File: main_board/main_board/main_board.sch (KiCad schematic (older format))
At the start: 9 parts, among them J1 jstsh4x1, J2 3.3v bus, J3 GND_bus, U1 Teensy3.5_All_Pins

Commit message: updated daughter board holes, should be good to fab
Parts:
- H1, H2, H3, H4: footprint exocam_charge_amp:mount_hole_2.5mm -> exocam_charge_amp:mount_hole_3mm
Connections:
- wire segments 31 -> 30
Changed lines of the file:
@@
 	1    0    0    -1
 $EndComp
-Wire Wire Line
-	3750 5300 3950 5300
 $Comp
 L power:GND #PWR0114
@@
 F 0 "H1" H 6900 2646 50  0000 L CNN
 F 1 "MountingHole-Mechanical" H 6900 2555 50  0000 L CNN
-F 2 "exocam_charge_amp:mount_hole_2.5mm" H 6800 2600 50  0001 C CNN
+F 2 "exocam_charge_amp:mount_hole_3mm" H 6800 2600 50  0001 C CNN
 F 3 "" H 6800 2600 50  0001 C CNN
 	1    6800 2600
@@
 F 0 "H2" H 6900 2896 50  0000 L CNN
 F 1 "MountingHole-Mechanical" H 6900 2805 50  0000 L CNN
-F 2 "exocam_charge_amp:mount_hole_2.5mm" H 6800 2850 50  0001 C CNN
+F 2 "exocam_charge_amp:mount_hole_3mm" H 6800 2850 50  0001 C CNN
 F 3 "" H 6800 2850 50  0001 C CNN
 	1    6800 2850
@@
 F 0 "H3" H 6900 3146 50  0000 L CNN
 F 1 "MountingHole-Mechanical" H 6900 3055 50  0000 L CNN
-F 2 "exocam_charge_amp:mount_hole_2.5mm" H 6800 3100 50  0001 C CNN
+F 2 "exocam_charge_amp:mount_hole_3mm" H 6800 3100 50  0001 C CNN
 F 3 "" H 6800 3100 50  0001 C CNN
 	1    6800 3100
@@
 F 0 "H4" H 6900 3396 50  0000 L CNN
 F 1 "MountingHole-Mechanical" H 6900 3305 50  0000 L CNN
-F 2 "exocam_charge_amp:mount_hole_2.5mm" H 6800 3350 50  0001 C CNN
+F 2 "exocam_charge_amp:mount_hole_3mm" H 6800 3350 50  0001 C CNN
 F 3 "" H 6800 3350 50  0001 C CNN
 	1    6800 3350
@@
 $EndComp
 Wire Wire Line
-	3950 5300 4500 5300
-Wire Wire Line
 	4750 5300 4750 5250
-Connection ~ 3950 5300
 $Comp
 L main_board-rescue:power_bus-exocam_charge_amp J3
@@
 Wire Wire Line
 	4500 5300 4750 5300
+Wire Wire Line
+	3750 5300 4500 5300
 $EndSCHEMATC

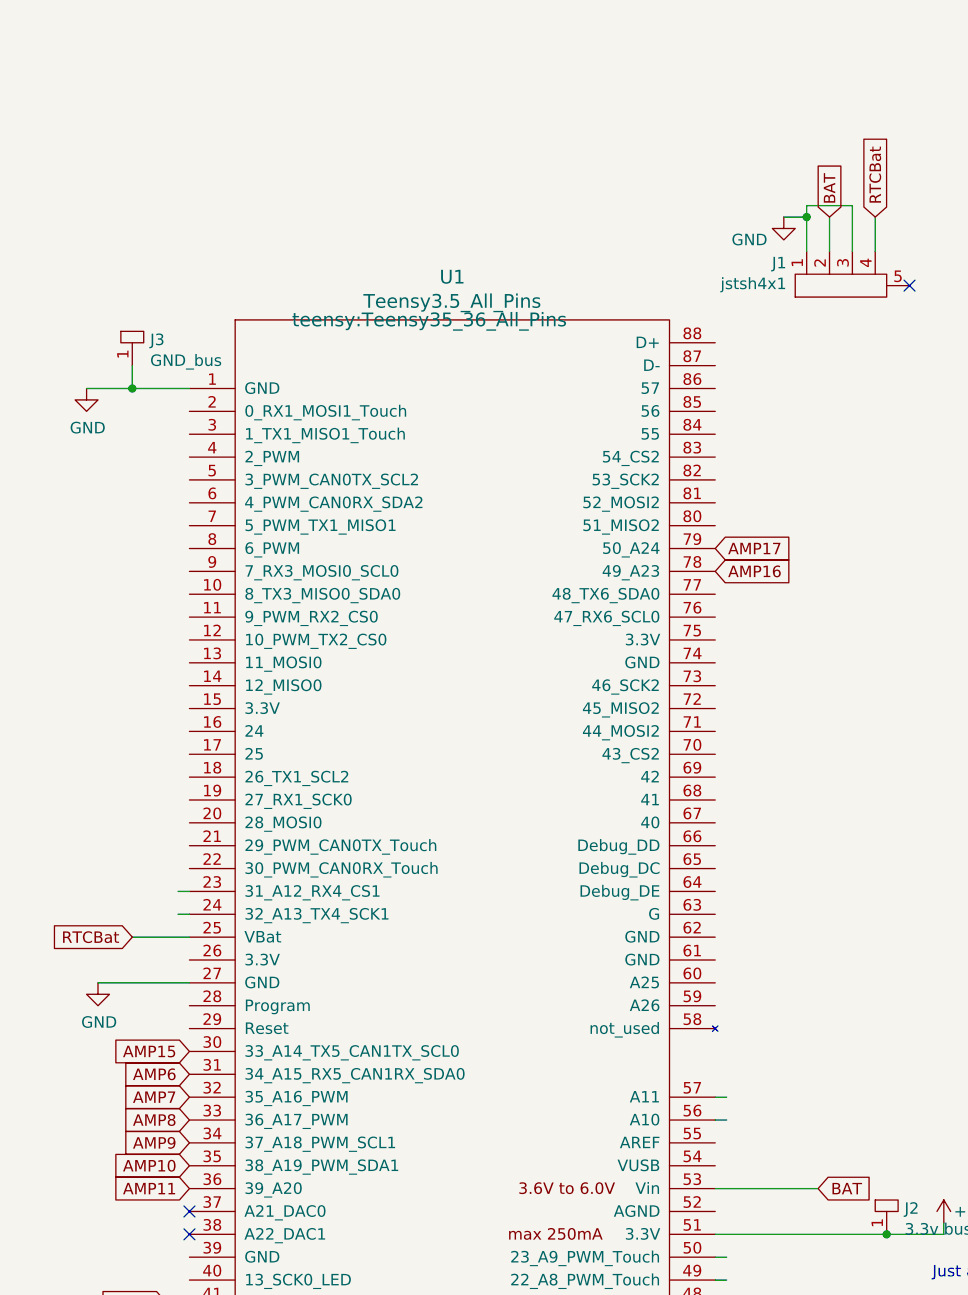
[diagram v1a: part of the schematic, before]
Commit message: edited daughter board schematic slightly to include the latest push button addition
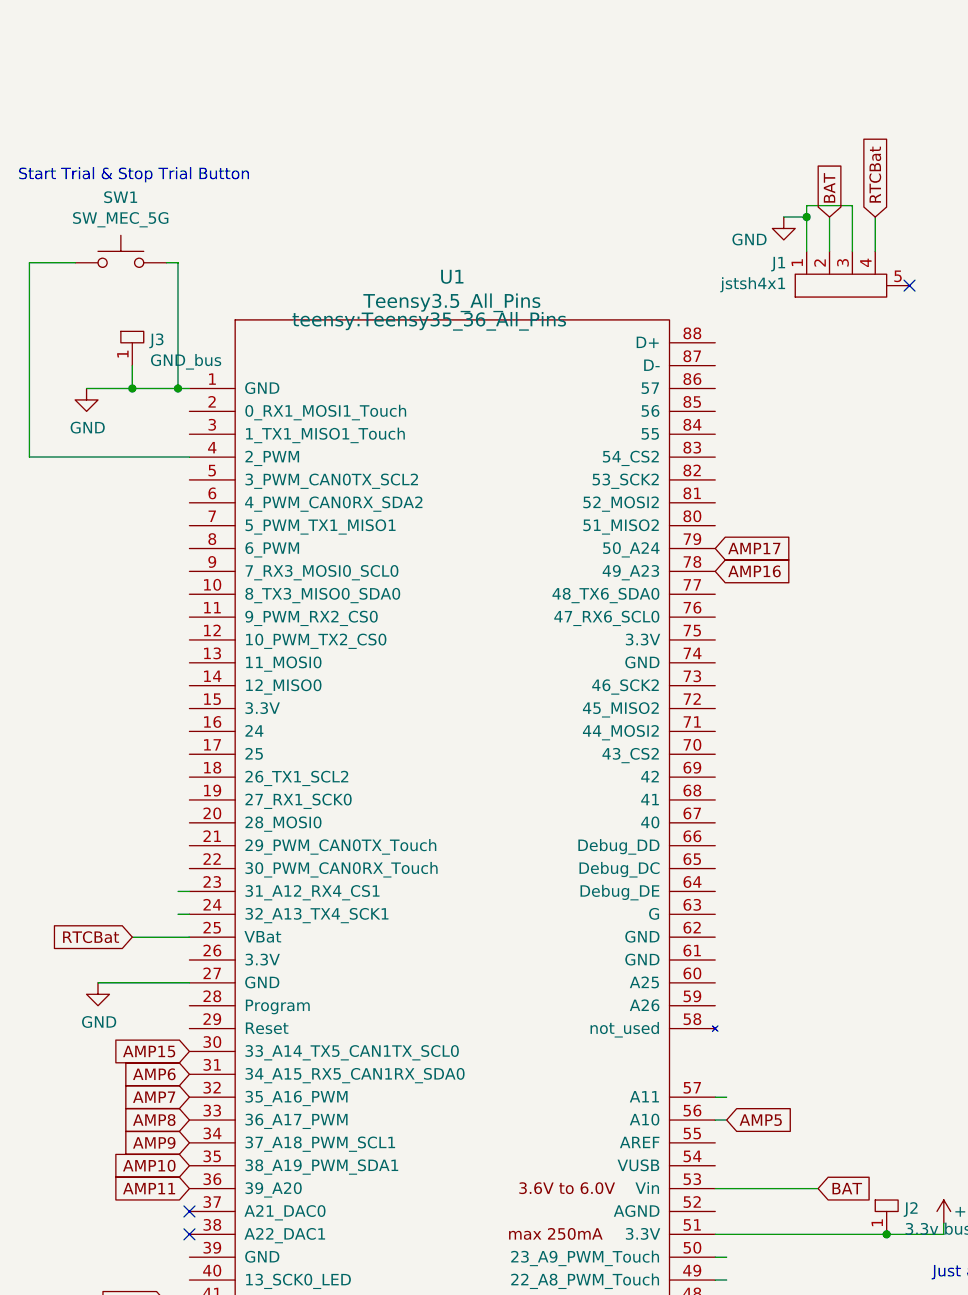
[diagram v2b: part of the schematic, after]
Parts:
- added SW1: SW_MEC_5G, symbol Switch:SW_MEC_5G
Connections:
- net labels added: AMP5
- wire segments 30 -> 36
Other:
- note added: "Start Trial & Stop Trial Button"
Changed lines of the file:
@@
 Connection ~ 1200 1600
 Wire Wire Line
-	1200 1600 1450 1600
+	1200 1600 1400 1600
 Text Notes 4700 5500 0    50   ~ 0
 Just a large ish pad that can be used for soldering a large number of wires.
@@
 Wire Wire Line
 	3750 5300 4500 5300
+Text GLabel 3800 4800 2    50   Input ~ 0
+AMP5
+$Comp
+L Switch:SW_MEC_5G SW1
+U 1 1 61235458
+P 1150 1050
+F 0 "SW1" H 1150 1335 50  0000 C CNN
+F 1 "SW_MEC_5G" H 1150 1244 50  0000 C CNN
+F 2 "" H 1150 1250 50  0001 C CNN
+F 3 "http://www.apem.com/int/index.php?controller=attachment&id_attachment=488" H 1150 1250 50  0001 C CNN
+	1    1150 1050
+	1    0    0    -1
+$EndComp
+Wire Wire Line
+	1400 1600 1400 1050
+Wire Wire Line
+	1400 1050 1350 1050
+Connection ~ 1400 1600
+Wire Wire Line
+	1400 1600 1450 1600
+Wire Wire Line
+	950  1050 750  1050
+Wire Wire Line
+	750  1050 750  1900
+Wire Wire Line
+	750  1900 1450 1900
+Text Notes 700  700  0    50   ~ 0
+Start Trial & Stop Trial Button
 $EndSCHEMATC

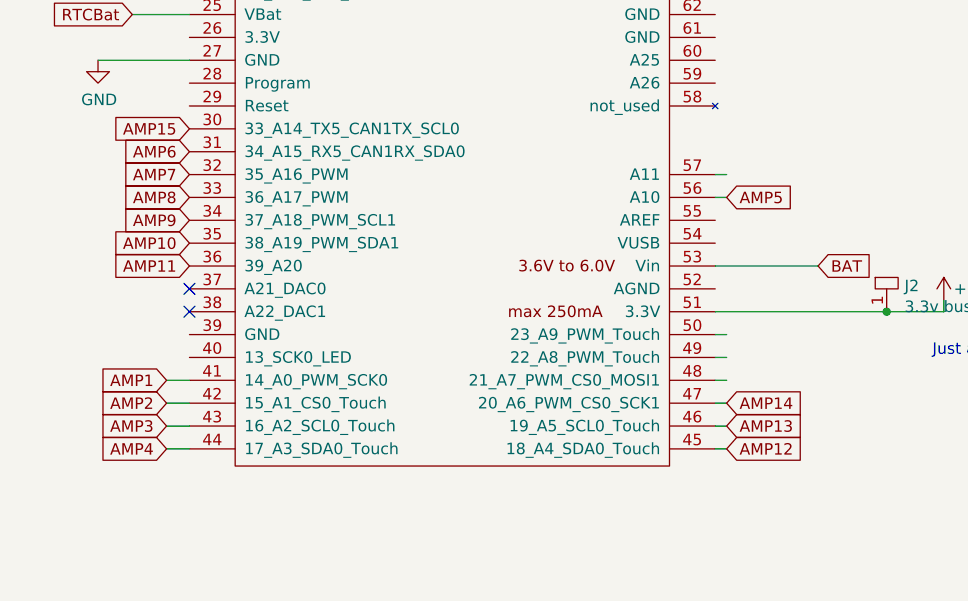
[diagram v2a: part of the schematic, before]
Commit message: updated pinout for daughter board (changed pin for AMP3)
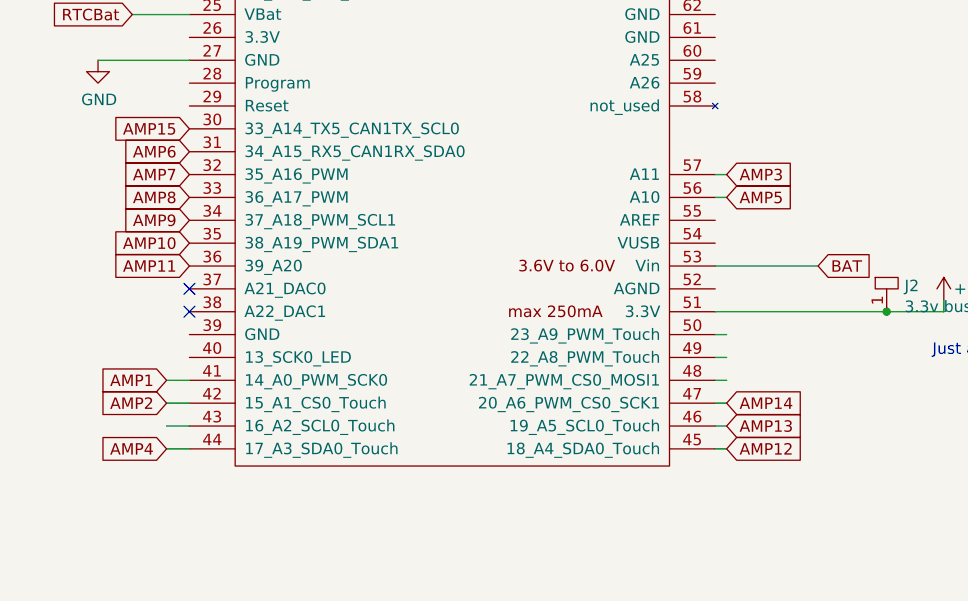
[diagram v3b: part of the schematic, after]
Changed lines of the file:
@@
 Wire Wire Line
 	1350 5700 1450 5700
-Text GLabel 1350 5800 0    50   Input ~ 0
-AMP3
 Wire Wire Line
 	1350 5800 1450 5800
@@
 Text Notes 700  700  0    50   ~ 0
 Start Trial & Stop Trial Button
+Text GLabel 3800 4700 2    50   Input ~ 0
+AMP3
 $EndSCHEMATC
